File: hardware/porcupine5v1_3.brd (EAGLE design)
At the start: 28.5 x 29.7 mm, 45 parts, among them X1 PROGCON

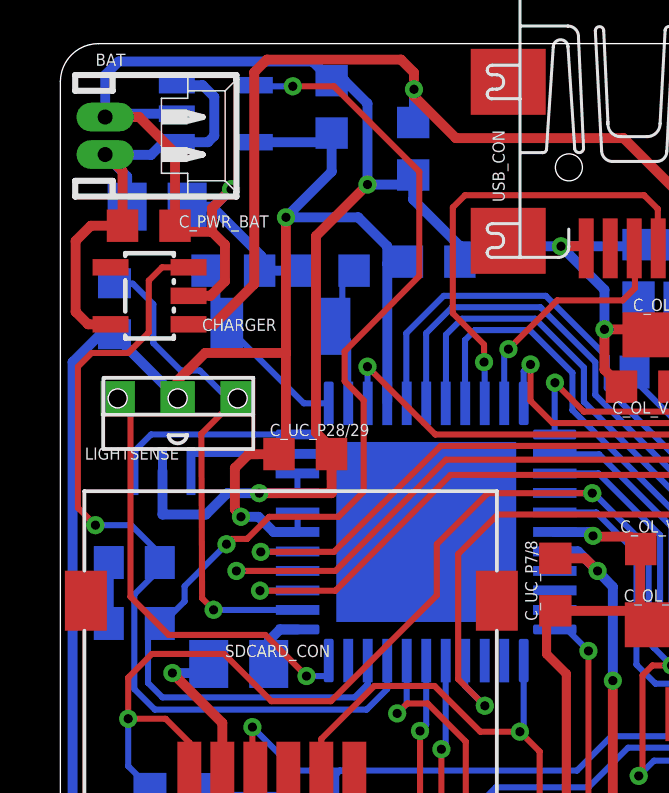
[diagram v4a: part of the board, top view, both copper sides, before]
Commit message: OLED BOM updated
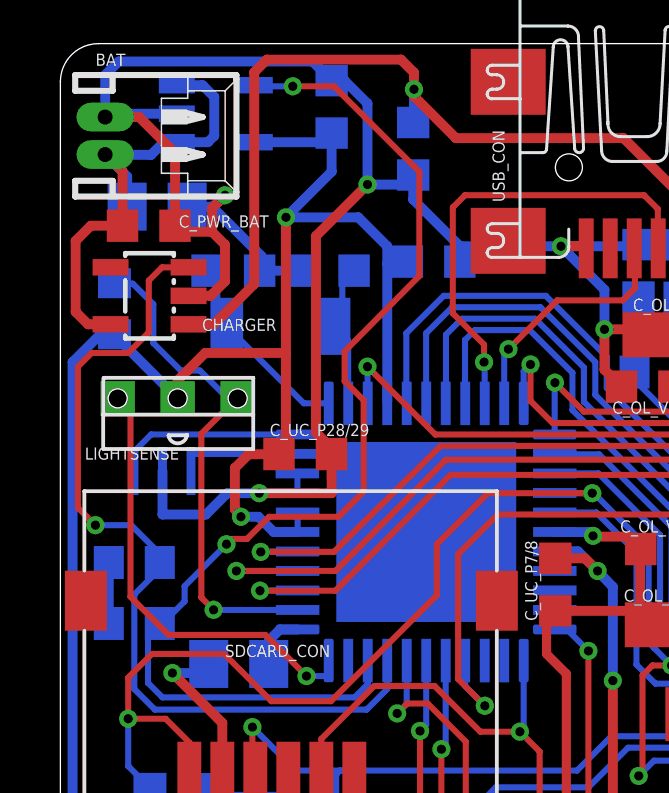
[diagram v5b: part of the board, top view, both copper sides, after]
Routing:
- net GND: track 195.0 -> 194.5 mm
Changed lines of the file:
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@@
 <grid distance="1" unitdist="mil" unit="mil" style="lines" multiple="1" display="yes" altdistance="0.025" altunitdist="inch" altunit="inch"/>
 <layers>
-<layer number="1" name="Top" color="4" fill="1" visible="no" active="yes"/>
-<layer number="16" name="Bottom" color="1" fill="1" visible="no" active="yes"/>
-<layer number="17" name="Pads" color="2" fill="1" visible="no" active="yes"/>
-<layer number="18" name="Vias" color="2" fill="1" visible="no" active="yes"/>
-<layer number="19" name="Unrouted" color="6" fill="1" visible="no" active="yes"/>
+<layer number="1" name="Top" color="4" fill="1" visible="yes" active="yes"/>
+<layer number="16" name="Bottom" color="1" fill="1" visible="yes" active="yes"/>
+<layer number="17" name="Pads" color="2" fill="1" visible="yes" active="yes"/>
+<layer number="18" name="Vias" color="2" fill="1" visible="yes" active="yes"/>
+<layer number="19" name="Unrouted" color="6" fill="1" visible="yes" active="yes"/>
 <layer number="20" name="Dimension" color="15" fill="1" visible="yes" active="yes"/>
-<layer number="21" name="tPlace" color="7" fill="1" visible="no" active="yes"/>
+<layer number="21" name="tPlace" color="7" fill="1" visible="yes" active="yes"/>
 <layer number="22" name="bPlace" color="7" fill="1" visible="yes" active="yes"/>
-<layer number="23" name="tOrigins" color="15" fill="1" visible="no" active="yes"/>
+<layer number="23" name="tOrigins" color="15" fill="1" visible="yes" active="yes"/>
 <layer number="24" name="bOrigins" color="15" fill="1" visible="yes" active="yes"/>
 <layer number="25" name="tNames" color="7" fill="1" visible="no" active="yes"/>
-<layer number="26" name="bNames" color="7" fill="1" visible="yes" active="yes"/>
+<layer number="26" name="bNames" color="7" fill="1" visible="no" active="yes"/>
 <layer number="27" name="tValues" color="7" fill="1" visible="no" active="yes"/>
 <layer number="28" name="bValues" color="7" fill="1" visible="no" active="yes"/>
@@
 <layer number="37" name="tTest" color="7" fill="1" visible="no" active="yes"/>
 <layer number="38" name="bTest" color="7" fill="1" visible="no" active="yes"/>
-<layer number="39" name="tKeepout" color="4" fill="11" visible="no" active="yes"/>
-<layer number="40" name="bKeepout" color="1" fill="11" visible="no" active="yes"/>
-<layer number="41" name="tRestrict" color="4" fill="10" visible="no" active="yes"/>
-<layer number="42" name="bRestrict" color="1" fill="10" visible="no" active="yes"/>
-<layer number="43" name="vRestrict" color="2" fill="10" visible="no" active="yes"/>
+<layer number="39" name="tKeepout" color="4" fill="11" visible="yes" active="yes"/>
+<layer number="40" name="bKeepout" color="1" fill="11" visible="yes" active="yes"/>
+<layer number="41" name="tRestrict" color="4" fill="10" visible="yes" active="yes"/>
+<layer number="42" name="bRestrict" color="1" fill="10" visible="yes" active="yes"/>
+<layer number="43" name="vRestrict" color="2" fill="10" visible="yes" active="yes"/>
 <layer number="44" name="Drills" color="7" fill="1" visible="no" active="yes"/>
 <layer number="45" name="Holes" color="7" fill="1" visible="yes" active="yes"/>
@@
 <wire x1="4.8514" y1="14.0208" x2="5.5626" y2="14.732" width="0.3302" layer="16"/>
 <wire x1="5.5626" y1="14.732" x2="6.6294" y2="14.732" width="0.3302" layer="16"/>
-<via x="5.6896" y="24.8666" extent="1-16" drill="0.3048" shape="octagon"/>
-<wire x1="5.6896" y1="24.8666" x2="5.0546" y2="24.2316" width="0.3302" layer="1"/>
+<via x="5.4864" y="24.6634" extent="1-16" drill="0.3048" shape="octagon"/>
+<wire x1="5.4864" y1="24.6634" x2="5.0546" y2="24.2316" width="0.3302" layer="1"/>
 <wire x1="5.0546" y1="24.2316" x2="5.0546" y2="23.4442" width="0.3302" layer="1"/>
-<wire x1="5.6896" y1="24.8666" x2="5.1054" y2="24.2824" width="0.3302" layer="16"/>
+<wire x1="5.4864" y1="24.6634" x2="5.1054" y2="24.2824" width="0.3302" layer="16"/>
 <wire x1="5.1054" y1="24.2824" x2="5.0546" y2="24.2824" width="0.3302" layer="16"/>
 <wire x1="4.9442" y1="9.0388" x2="4.7026" y2="8.734" width="0.3302" layer="16"/>
@@
 <wire x1="5.1054" y1="10.8458" x2="5.1244" y2="10.8394" width="0.2032" layer="16"/>
 <wire x1="5.1244" y1="10.8394" x2="7.9073" y2="10.8394" width="0.2032" layer="16"/>
-<wire x1="5.1054" y1="10.8458" x2="4.7244" y2="11.2268" width="0.2032" layer="1"/>
-<wire x1="4.7244" y1="11.2268" x2="4.699" y2="16.7132" width="0.2032" layer="1"/>
+<wire x1="5.1054" y1="10.8458" x2="4.699" y2="11.2522" width="0.2032" layer="1"/>
+<wire x1="4.699" y1="11.2522" x2="4.699" y2="16.7132" width="0.2032" layer="1"/>
 <wire x1="4.699" y1="16.7132" x2="5.8826" y2="17.8968" width="0.2032" layer="1"/>
 <wire x1="5.8826" y1="17.8968" x2="5.908" y2="17.892" width="0.2032" layer="1"/>
